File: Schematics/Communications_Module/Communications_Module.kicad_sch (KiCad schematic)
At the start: 72 parts, among them J1 USB_B_Micro, J2 SWD_01x04_Pin, J3 Stack Male Edge Connector, Q1 AO3400A, SW1 SW_STM_RESET, SW2 SW_STM_BOOT_MODE, U1 RFM95W-915S2, U2 W25Q128JVS, U3 AMS1117-3.3, U4 LM66100DCKR, U5 LM66100DCKR, U6 LM66100DCKR, U7 STM32F103CBT6, U8 ACS70331EOLC, U9 ISO1042BDWVR, Y1 X322516MMB4SI

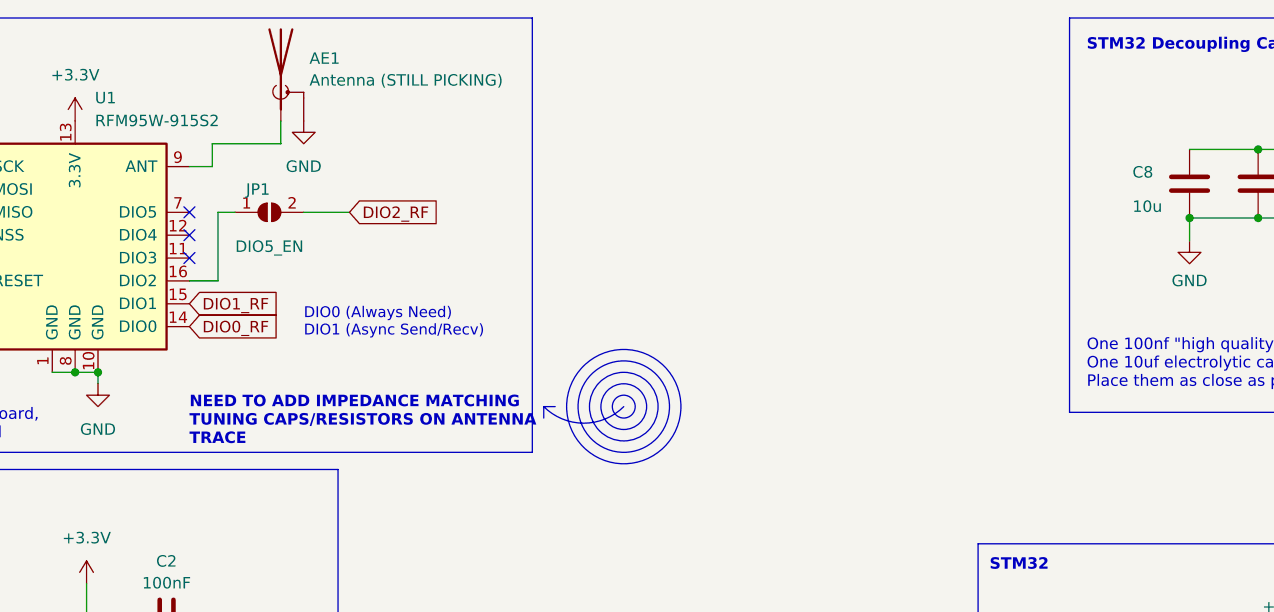
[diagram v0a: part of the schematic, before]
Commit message: Added note about antenna
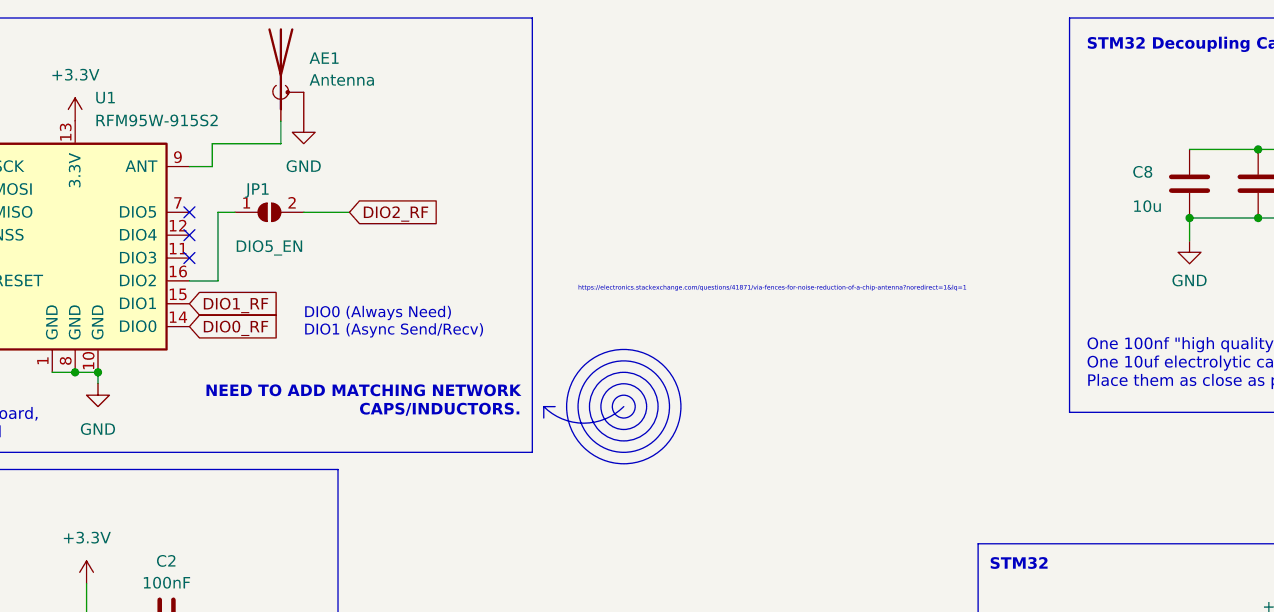
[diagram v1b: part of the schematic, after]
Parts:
- AE1: value Antenna (STILL PICKING) -> Antenna
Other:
- note added: "NEED TO ADD MATCHING NETWORK CAPS/INDUCTORS."
- note added: "https://electronics.stackexchange.com/questions/41871/via-fences-for-noise-reduction-of-a-chip-antenna?noredirect=1&lq=1"
- note removed: "NEED TO ADD IMPEDANCE MATCHING TUNING CAPS/RESISTORS ON ANTENNA TRACE"

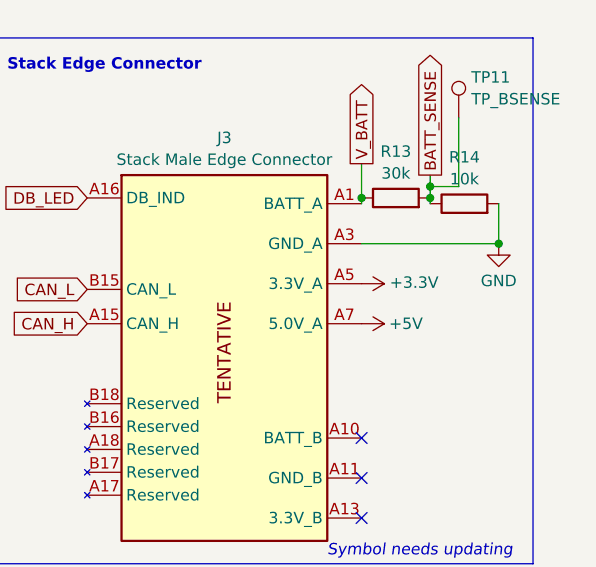
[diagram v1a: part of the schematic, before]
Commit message: Added flash LCSC # and fixed stack connector pinout
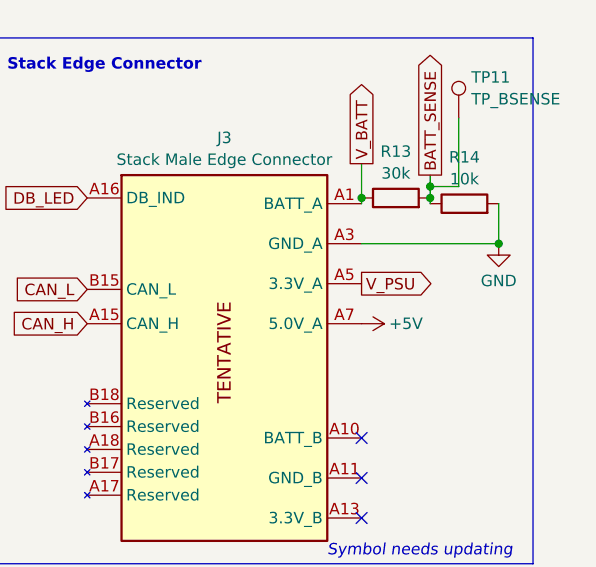
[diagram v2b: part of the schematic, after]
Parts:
- U2: LCSC (none) -> C97521
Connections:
- net +3.3V: no longer J3.A5 (3.3V_A), J3.B5 (3.3V_A)
- net V_PSU: now also J3.A5 (3.3V_A), J3.B5 (3.3V_A)
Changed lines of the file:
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@@
   (title_block
     (title "QRET 23-24 SRAD Communications Module")
-    (date "2024-03-03")
+    (date "2024-03-07")
     (rev "V0.3.0")
     (company "Queen's Rocket Engineering Team")
@@
     )
   )
+  (global_label "V_PSU" (shape output) (at 398.78 154.305 0) (fields_autoplaced)
+    (effects (font (size 1.27 1.27)) (justify left))
+    (property "Intersheetrefs" "${INTERSHEET_REFS}" (at 407.6314 154.305 0)
+      (effects (font (size 1.27 1.27)) (justify left) hide)
+    )
+  )
   (global_label "V_SWD" (shape output) (at 26.67 211.455 180) (fields_autoplaced)
     (effects (font (size 1.27 1.27)) (justify right))
@@
     )
   )
-  (symbol (lib_id "power:+3.3V") (at 398.78 154.305 270) (unit 1)
-    (in_bom yes) (on_board yes) (dnp no)
-    (property "Reference" "#PWR048" (at 394.97 154.305 0)
-      (effects (font (size 1.27 1.27)) hide)
-    )
-    (property "Value" "+3.3V" (at 404.622 154.178 90)
-      (effects (font (size 1.27 1.27)))
-    )
-    (property "Footprint" "" (at 398.78 154.305 0)
-      (effects (font (size 1.27 1.27)) hide)
-    )
-    (property "Datasheet" "" (at 398.78 154.305 0)
-      (effects (font (size 1.27 1.27)) hide)
-    )
-    (pin "1")
-    (instances
-      (project "Communications_Module"
-        (path "/ace06731-9b48-45c3-868d-c65fed1a8f9b"
-          (reference "#PWR048") (unit 1)
-        )
-      )
-      (project "processor"
-        (path "/ccfbe2af-01d0-4f8a-8e0b-98df5d6602a9"
-          (reference "#PWR?") (unit 1)
-        )
-      )
-    )
-  )
   (symbol (lib_id "Device:R") (at 373.38 104.14 270) (unit 1)
     (in_bom yes) (on_board yes) (dnp no) (fields_autoplaced)
@@
       (effects (font (size 1.27 1.27)) hide)
     )
+    (property "LCSC" "C97521" (at 54.61 94.615 0)
+      (effects (font (size 1.27 1.27)) hide)
+    )

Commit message: Switched LM66100 footprints to hand-solderable ones
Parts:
- U4, U5, U6: footprint LMR66100:SC-70-6 -> LMR66100:SC-70-6_Handsoldering
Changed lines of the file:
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@@
       (effects (font (size 1.524 1.524)))
     )
-    (property "Footprint" "LMR66100:SC-70-6" (at 121.92 215.265 0)
+    (property "Footprint" "LMR66100:SC-70-6_Handsoldering" (at 121.92 215.265 0)
       (effects (font (size 1.27 1.27) italic) hide)
     )
@@
       (effects (font (size 1.524 1.524)))
     )
-    (property "Footprint" "LMR66100:SC-70-6" (at 121.92 253.365 0)
+    (property "Footprint" "LMR66100:SC-70-6_Handsoldering" (at 121.92 253.365 0)
       (effects (font (size 1.27 1.27) italic) hide)
     )
@@
       (effects (font (size 1.524 1.524)))
     )
-    (property "Footprint" "LMR66100:SC-70-6" (at 121.92 234.315 0)
+    (property "Footprint" "LMR66100:SC-70-6_Handsoldering" (at 121.92 234.315 0)
       (effects (font (size 1.27 1.27) italic) hide)
     )

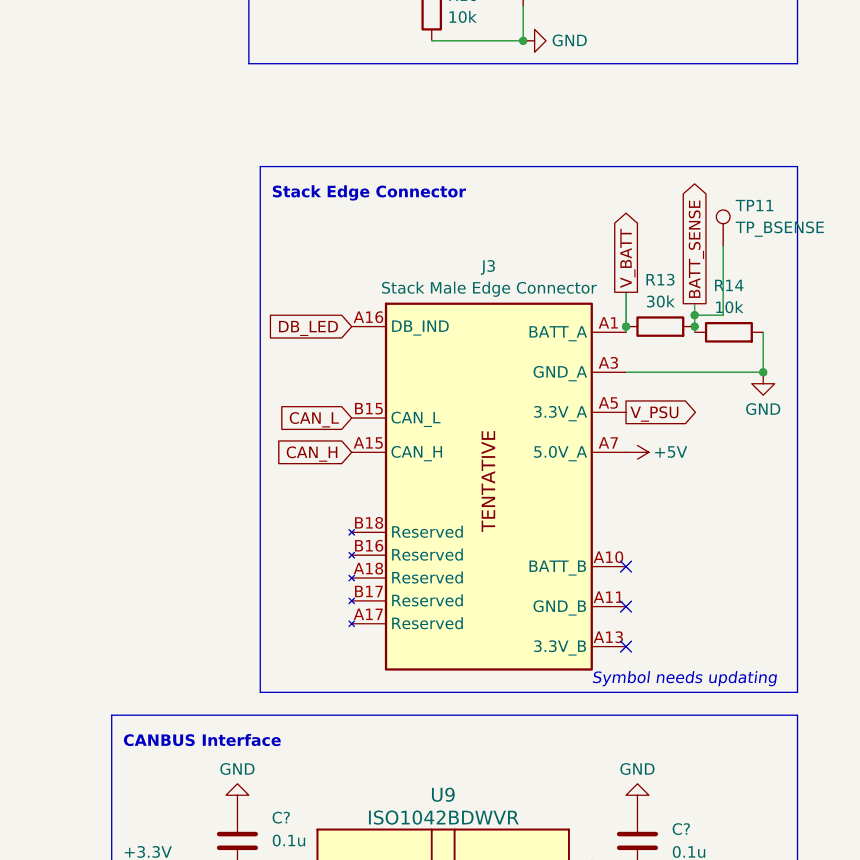
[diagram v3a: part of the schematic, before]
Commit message: Updated stack edge connector (V1)
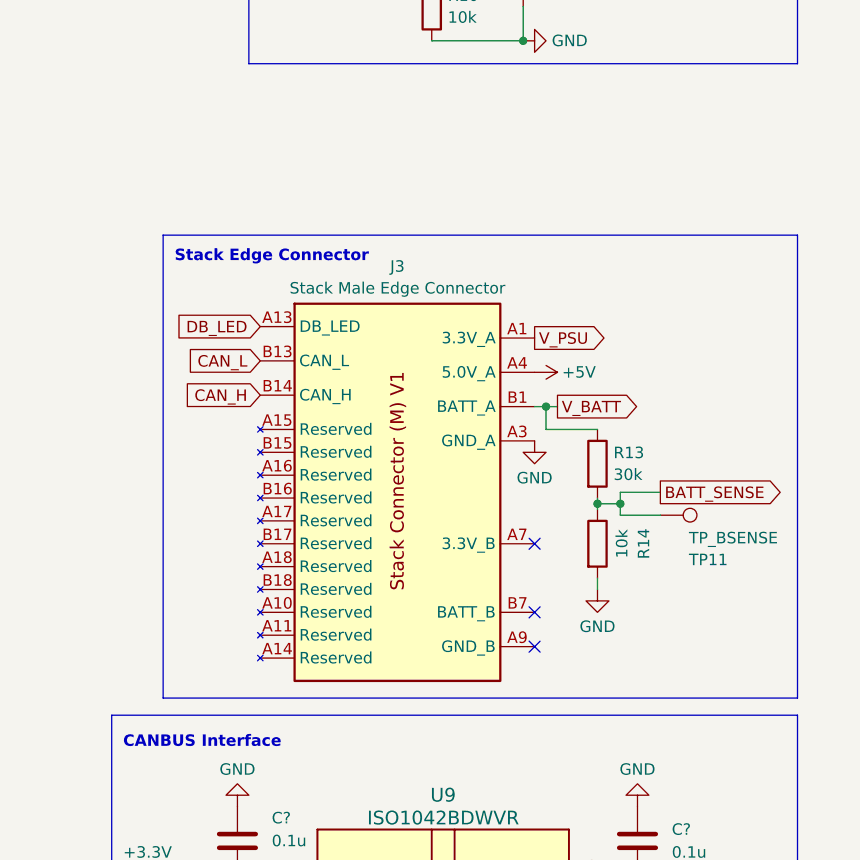
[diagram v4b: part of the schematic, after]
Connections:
- net +5V: now also J3.A4 (5.0V_A), J3.A5 (5.0V_A); no longer J3.A7 (5.0V_A), J3.B7 (5.0V_A)
- net CAN_H: now also J3.B14 (CAN_H); no longer J3.A15 (CAN_H)
- net CAN_L: now also J3.B13 (CAN_L); no longer J3.B15 (CAN_L)
- net DB_LED: now also J3.A13 (DB_LED); no longer J3.A16 (DB_IND)
- net GND: now also J3.B5 (GND_A); no longer J3.A4 (GND_A), J3.A8 (GND_A), J3.B3 (GND_A), J3.B8 (GND_A)
- net V_BATT: now also J3.B3 (BATT_A); no longer J3.A1 (BATT_A), J3.A2 (BATT_A)
- net V_PSU: now also J3.A1 (3.3V_A), J3.A2 (3.3V_A); no longer J3.A5 (3.3V_A), J3.B5 (3.3V_A)
- net at J3.A9 (GND_B), J3.B10 (GND_B): now also J3.A12 (GND_B), J3.B11 (GND_B), J3.B12 (GND_B); no longer J3.A10 (BATT_B), J3.B9 (BATT_B)
- new net: J3.A7 (3.3V_B), J3.A8 (3.3V_B)
- new net: J3.B7 (BATT_B), J3.B8 (BATT_B), J3.B9 (BATT_B)
- now unconnected: J3.A11 (GND_B), J3.A14 (GND_B)
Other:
- note removed: "Symbol needs updating"
- moved on the sheet: R13, R14, TP11

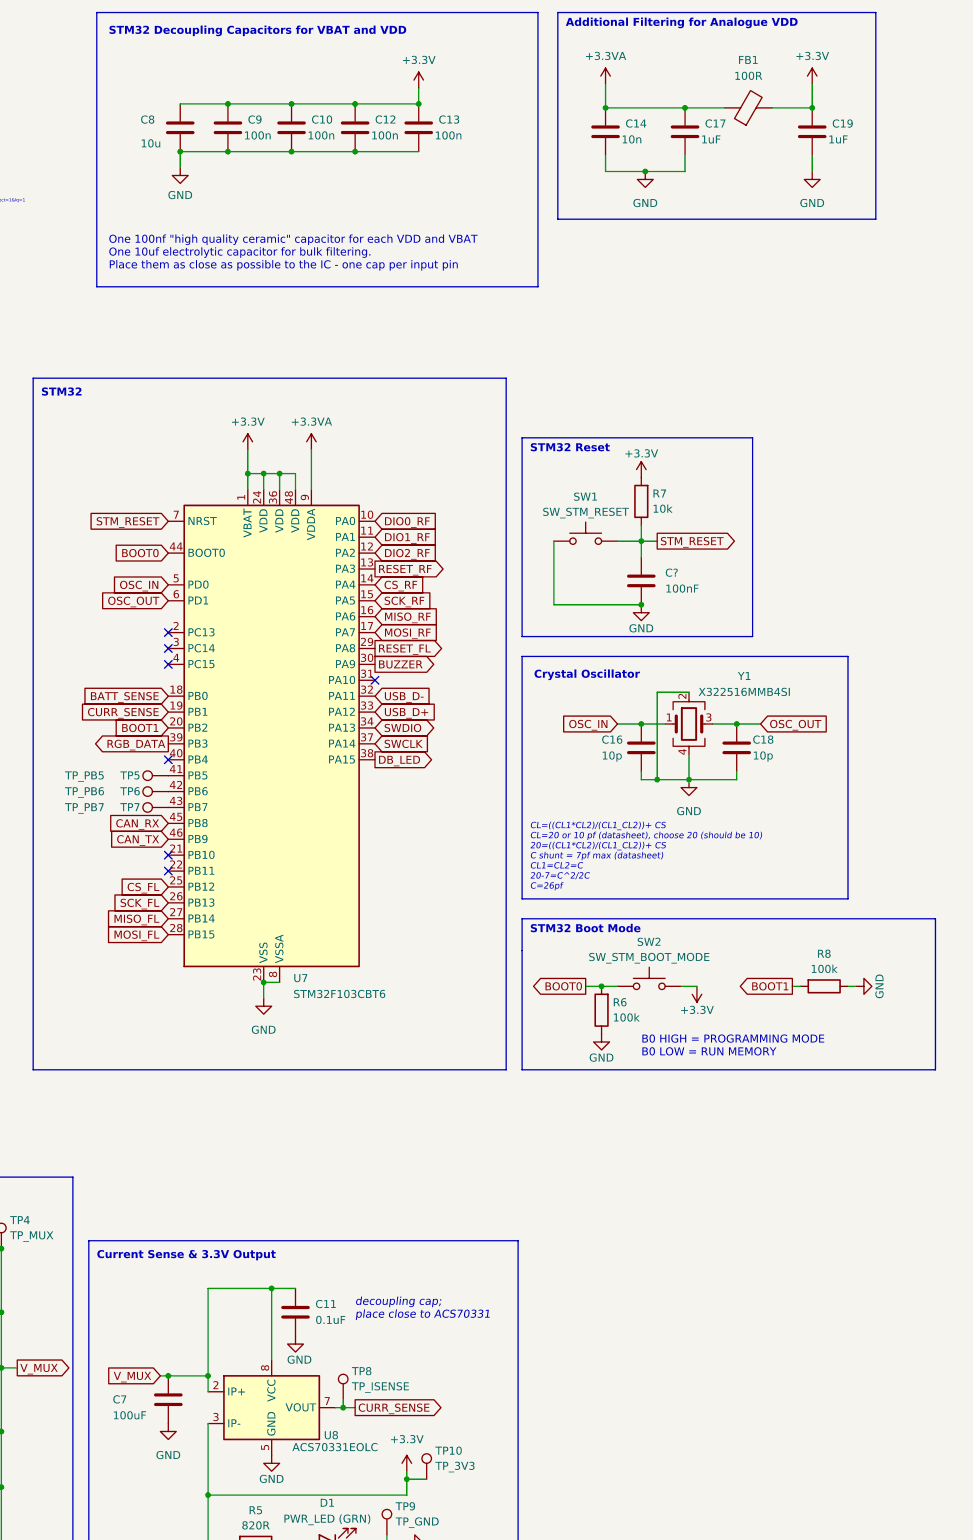
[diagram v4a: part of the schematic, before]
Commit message: Updated symbols for electrolytic capacitors
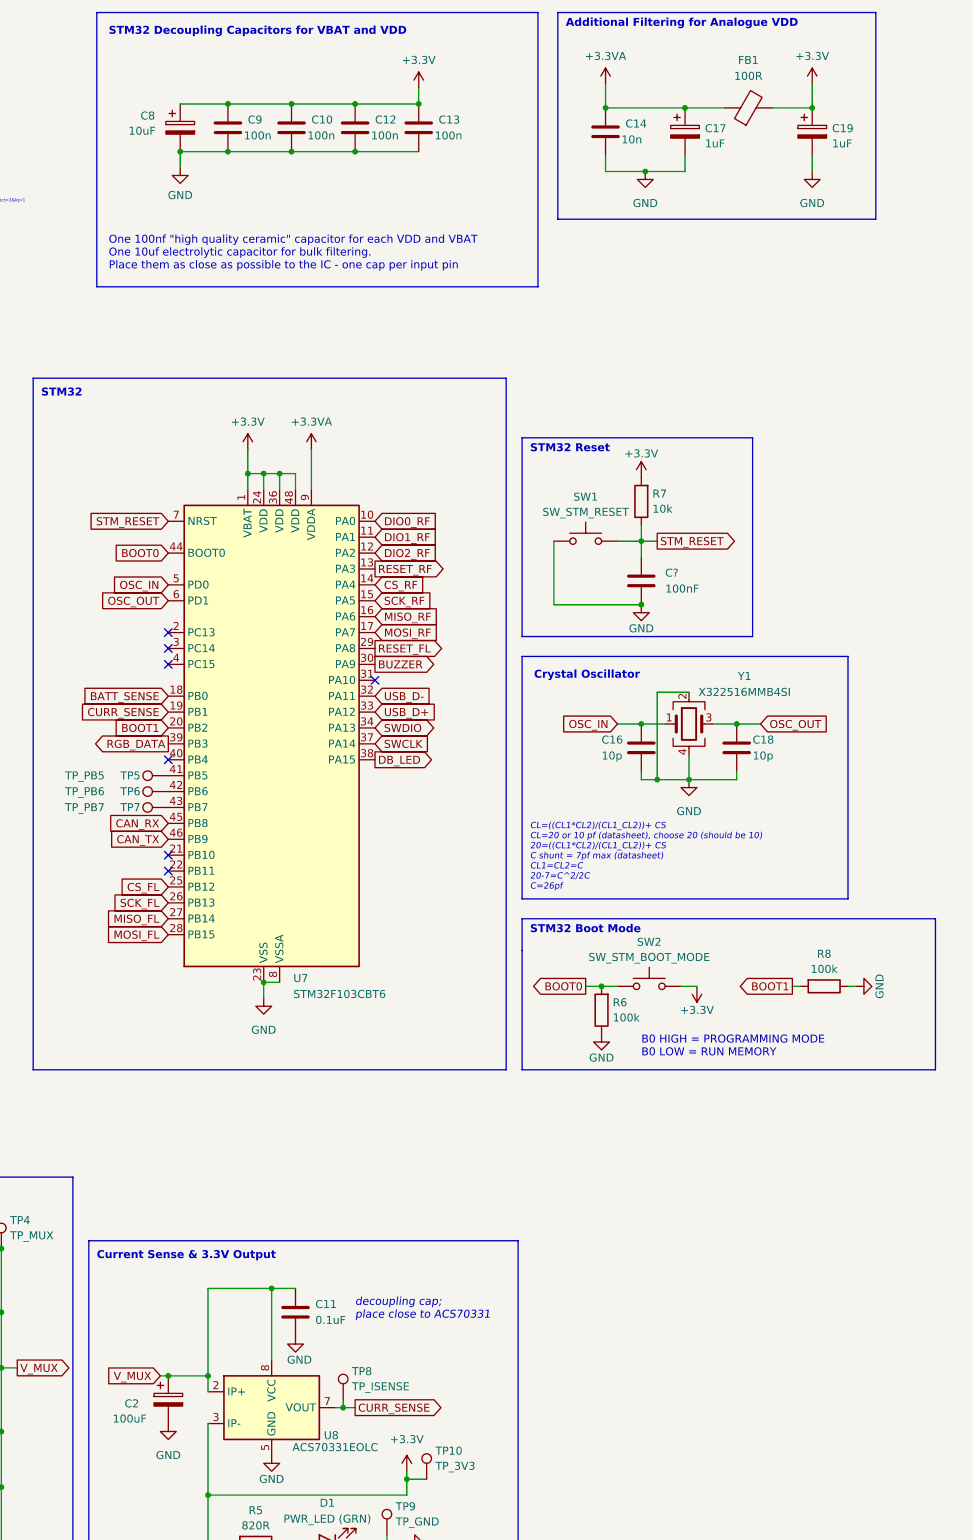
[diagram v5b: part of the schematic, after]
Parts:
- removed C17, C19: 1uF, Capacitor_SMD:CP_Elec_4x5.4, symbol Device:C
- removed C7: 100uF, Capacitor_SMD:CP_Elec_6.3x5.9, symbol Device:C
- removed C8: 10u, Capacitor_SMD:CP_Elec_4x5.4, symbol Device:C
- added C17, C19: 1uF, Capacitor_SMD:CP_Elec_4x5.4, symbol Device:C_Polarized
- added C2: 100uF, Capacitor_SMD:CP_Elec_6.3x5.9, symbol Device:C_Polarized
- added C8: 10uF, Capacitor_SMD:CP_Elec_4x5.4, symbol Device:C_Polarized
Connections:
- net +3.3V: now also C19.1, C8.1
- net +3.3VA: now also C17.1
- net GND: now also C17.2, C19.2, C2.2, C8.2
- net V_MUX: now also C2.1
